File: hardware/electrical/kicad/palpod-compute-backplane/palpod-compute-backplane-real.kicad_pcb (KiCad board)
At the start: 4 copper layers, 450 x 300 mm, 40 parts, among them J1 MM70_260_SODIMM (Jetson Orin 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, J10 MM70_260_SODIMM (Jetson Orin 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, J11 SAMTEC_EXAMAX_200 (Ryzen AI 9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, J12 SAMTEC_EXAMAX_200 (Ryzen AI 9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, J13 SAMTEC_EXAMAX_200 (Ryzen AI 9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, J14 SAMTEC_EXAMAX_200 (Ryzen AI 9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, J15 SAMTEC_EXAMAX_200 (Ryzen AI 9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, J16 SAMTEC_EXAMAX_200 (Ryzen AI 9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, J17 SAMTEC_EXAMAX_200 (Ryzen AI 9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, J18 SAMTEC_EXAMAX_200 (Ryzen AI 9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, J19 SAMTEC_EXAMAX_200 (Ryzen AI 9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, J2 MM70_260_SODIMM (Jetson Orin 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, J20 SAMTEC_EXAMAX_200 (Ryzen AI 9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, J21 ATX24 (+12V PSU input), J22 ATX24 (+12V PSU input B), J3 MM70_260_SODIMM (Jetson Orin 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, J4 MM70_260_SODIMM (Jetson Orin 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, J5 MM70_260_SODIMM (Jetson Orin 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, J6 MM70_260_SODIMM (Jetson Orin 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, J7 MM70_260_SODIMM (Jetson Orin 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, J8 MM70_260_SODIMM (Jetson Orin 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, J9 MM70_260_SODIMM (Jetson Orin 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, U1 BCM56780 (Trident 4 12.8Tbps), U2 ARIES_PT4 (PCIe Gen5 retimer), U3 UCD90320 (32-rail sequencer), U4 NCT6116 (BMC / super-I/O), U5 SLB9670 (TPM 2.0), U6 TPS543x (12V -> 5V, 15A)

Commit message: brand: sweep KiCad silkscreen + title metadata + Hey Pod wake word to Hearth
Follow-up to 3184563 rebrand sweep. Verifier caught KiCad title/company/
silkscreen "PAL Pod" strings that would be etched on physical PCBs if
fabricated — critical exposure.

Changes:
- .kicad_sch / .kicad_pcb / .kicad_pro title + company fields → Hearth /
  Hearth Home, Inc.
- gr_text silkscreen on F.SilkS layer → Hearth Orb - Rev A0 (physical)
- fp-lib-table + sym-lib-table description strings
- Wake word Hey Pod → Hey Hearth across all user-facing .md + .html

Not changed (still internal codenames per rebrand rules):
- Filenames (palpod-orb.kicad_sch etc.)
- Directory names (palpod-orb/, pal-web/, pal-voice/, pal-face/)
- Code identifiers (palpod_csrf, palpod_session, palpod_agent_token)
- Docker service names
- Wake-word ONNX model filename (hey_pod.onnx internally)
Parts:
- gave numbers to parts that had none: 6

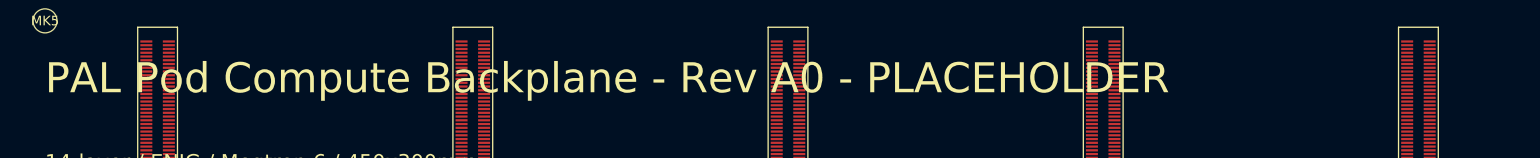
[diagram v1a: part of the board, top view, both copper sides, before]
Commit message: brand: broad KiCad sweep — remaining PAL Pod strings → Hearth
Targeted-pattern sed in ff14a48 missed variants. Broad find-replace
on .kicad_sch/pcb/pro/sym/mod + fp-lib-table + sym-lib-table +
per-project README.md (only where PAL Pod string actually appeared).
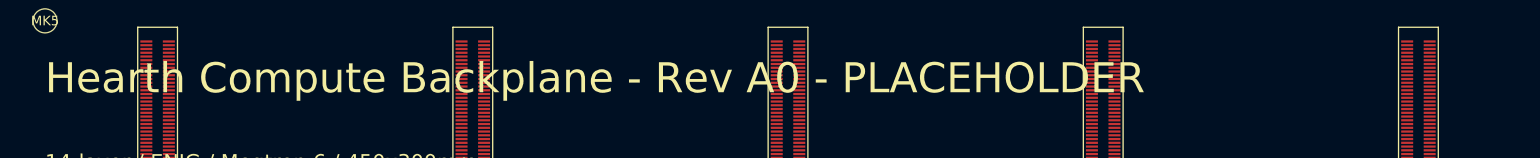
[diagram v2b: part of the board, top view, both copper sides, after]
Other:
- board text added: "Hearth Compute Backplane - Rev A0 - PLACEHOLDER"
- board text removed: "PAL Pod Compute Backplane - Rev A0 - PLACEHOLDER"
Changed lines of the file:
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@@
 	(paper "A2")
 	(title_block
-		(title "PAL Pod Compute Backplane - PCB")
+		(title "Hearth Compute Backplane - PCB")
 		(date "2026-08-03")
 		(rev "A0")
@@
 		)
 	)
-	(gr_text "PAL Pod Compute Backplane - Rev A0 - PLACEHOLDER"
+	(gr_text "Hearth Compute Backplane - Rev A0 - PLACEHOLDER"
 		(at 225 20 0)
 		(layer "F.SilkS")
